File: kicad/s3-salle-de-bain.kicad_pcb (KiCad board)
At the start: 2 copper layers, 135 x 100 mm, 22 parts, among them J1 Jack-3.5mm, J2 USB-C, Q1 AO3401, SW1 EC11, SW2 Mute-SPDT, U1 ESP32-S3-DevKitC-1, U2 GY-PCM5102, U3 PAM8403, U4 INMP441, U5 AMS1117-3.3

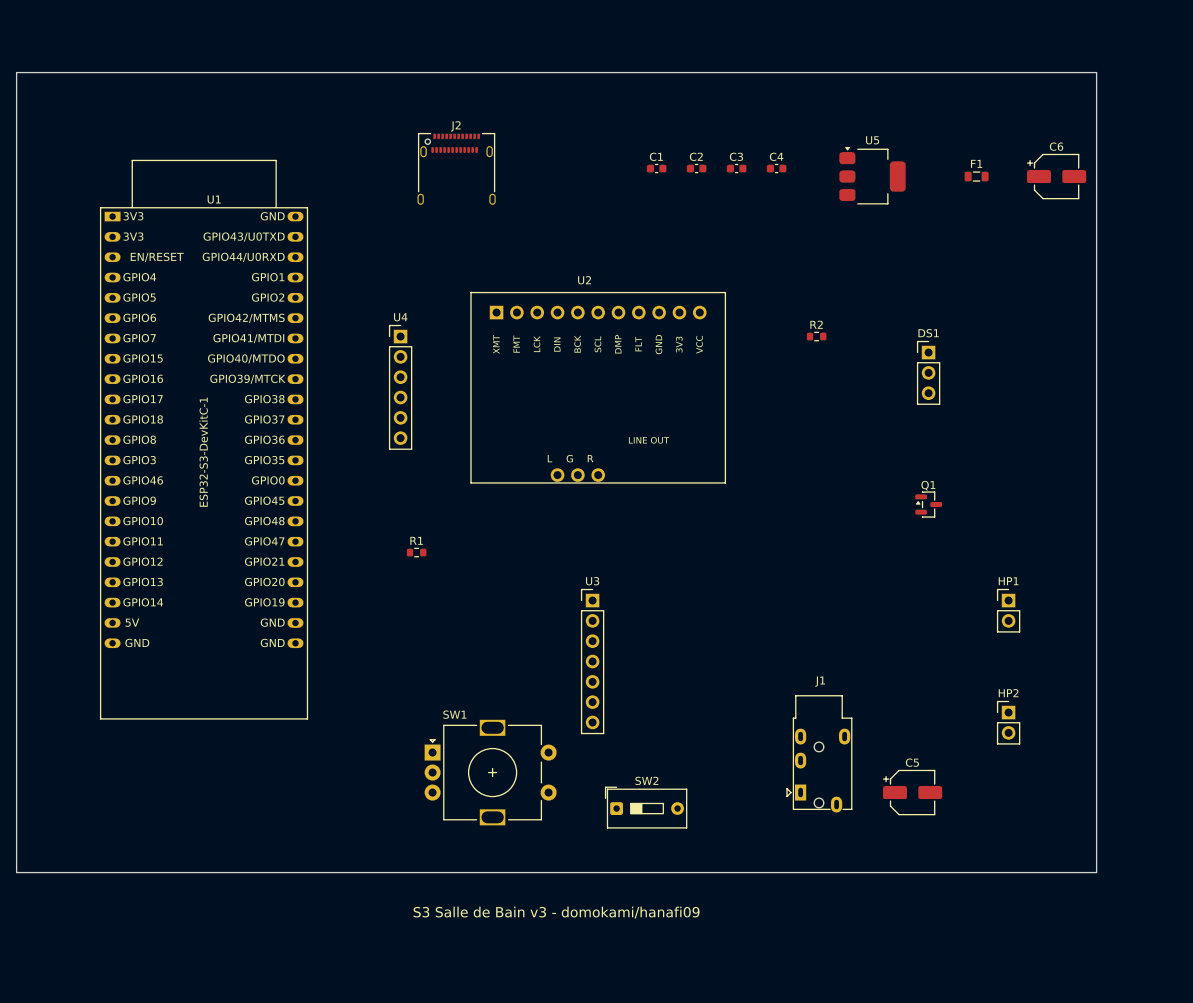
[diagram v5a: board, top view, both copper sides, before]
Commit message: fix(pcb): real INMP441 + PAM8403 module footprints (from photos)
- GY-INMP441 round footprint (2x3: L/R WS SCK / SD VDD GND)
- PAM8403-mini footprint (BTL out L-/L+/R-/R+, audio in L/G/R, power +/-)
- Speakers now wired differential (SPK_L+/L-, SPK_R+/R-) not to GND
- Add Q2 P-MOSFET amp power-gate (GPIO47 enables PAM8403, no SHDN on module)
- New +5V_AMP gated rail
- Schematic symbols + footprint properties updated to match
- Board widened to 145x108mm, DRC: 0 errors
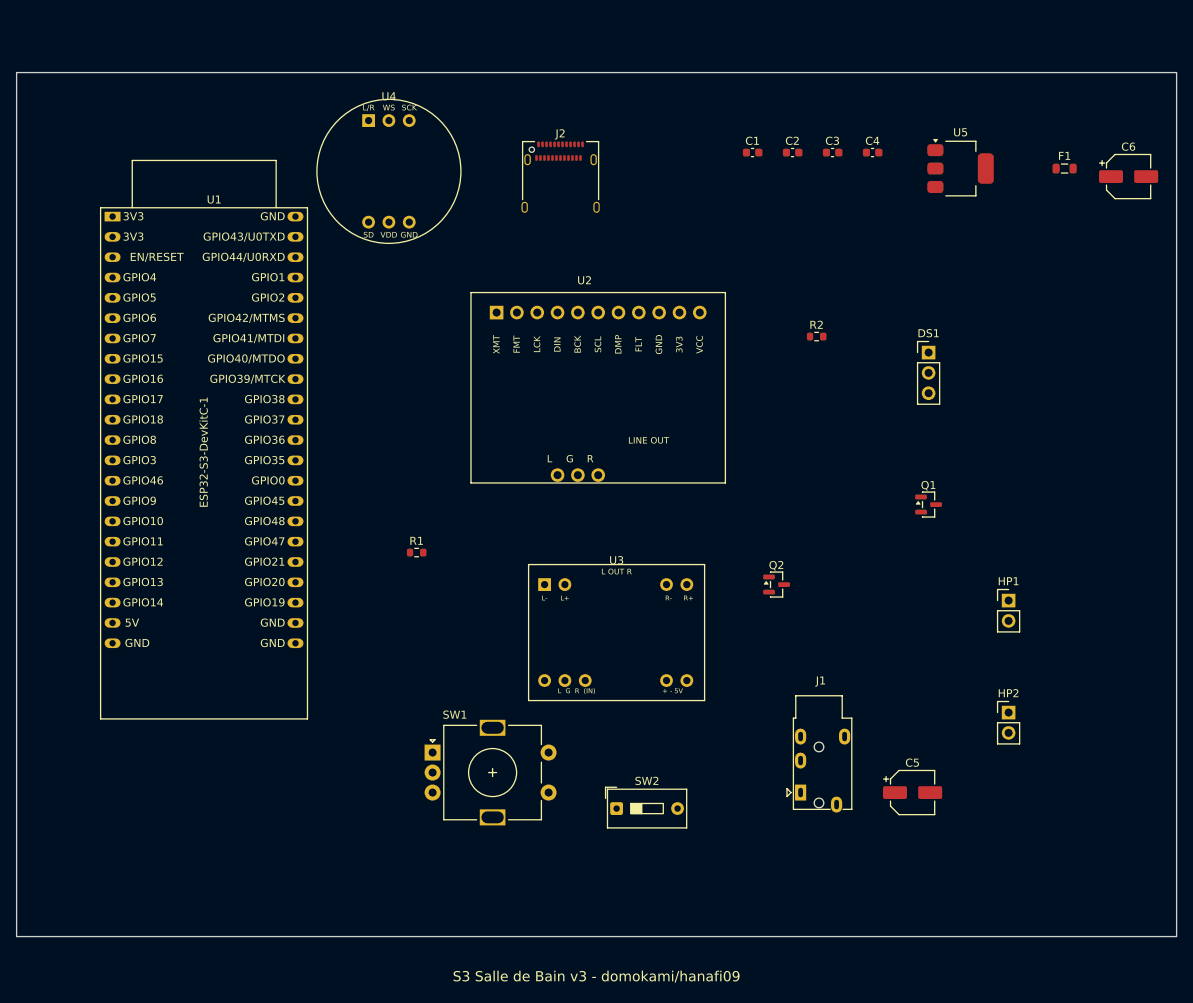
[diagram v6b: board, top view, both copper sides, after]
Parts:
- added Q2: AO3401, SOT-23, F.Cu at (95.0, 64.0)
- U3: footprint PinHeader_1x07_P2.54mm_Vertical -> PAM8403-mini
- U4: footprint PinHeader_1x06_P2.54mm_Vertical -> GY-INMP441
- moved U4 27.3 mm to (44.0, 6.00)
- moved J2 13.0 mm to (68.0, 14.0)
- moved C1 12.2 mm to (92.0, 10.0)
- moved C2 12.2 mm to (97.0, 10.0)
- moved C3 12.2 mm to (102.0, 10.0)
- moved C4 12.2 mm to (107.0, 10.0)
- moved F1 11.0 mm to (131.0, 12.0)
- moved U5 11.0 mm to (118.0, 12.0)
- moved C6 9.00 mm to (139.0, 13.0)
- moved U3 6.32 mm to (66.0, 64.0)
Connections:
- HP1 pad 1: SPK_L -> SPK_L+
- HP1 pad 2: GND -> SPK_L-
- HP2 pad 1: SPK_R -> SPK_R+
- HP2 pad 2: GND -> SPK_R-
- U4 pad 1: +3V3 -> GND
- U4 pad 2: GND -> MIC_LRCLK
- U4 pad 3: GND -> MIC_BCLK
- U4 pad 4: MIC_LRCLK -> MIC_DIN
- U4 pad 5: MIC_BCLK -> +3V3
- U4 pad 6: MIC_DIN -> GND
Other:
- board size 135 x 100 mm -> 145 x 108 mm
